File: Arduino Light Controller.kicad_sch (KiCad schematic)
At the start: 26 parts, among them J1 61300411121, J10 61300211121, J11 61300211121, J12 61300211121, J13 61300211121, J14 61300211121, J15 61300211121, J16 61300211121, J17 61300211121, J18 61300211121, J19 61300211121, J2 61300411121, J20 61300211121, J21 61300211121, J22 61300211121, J3 61300411121, J4 61300411121, J5 61300311121, J6 61300311121, J7 61300211121, J8 61300211121, J9 61300211121

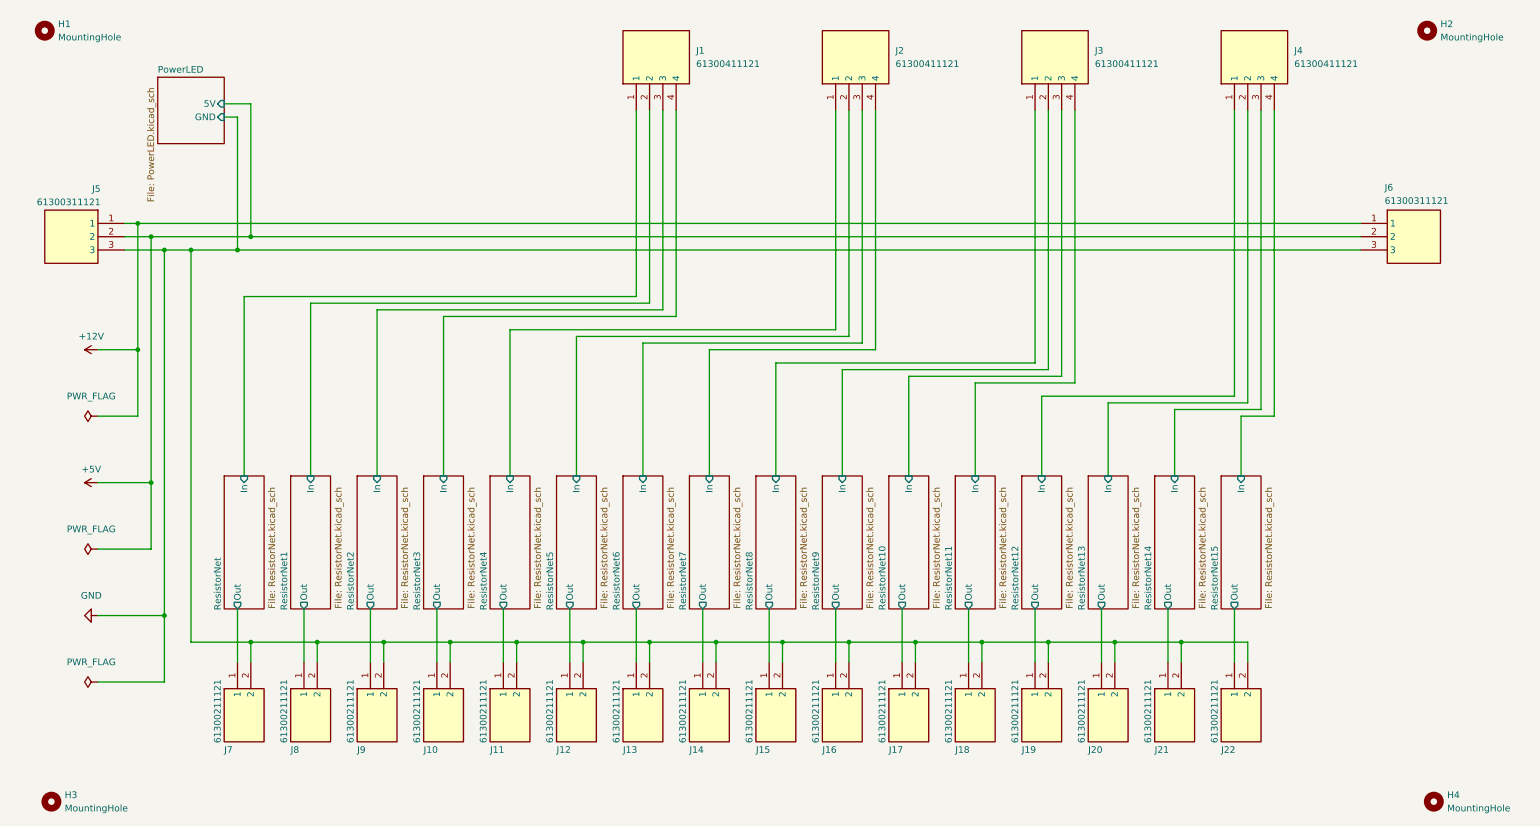
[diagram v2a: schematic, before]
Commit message: Updated re-annotated the schematics, created new PCB based on standards and updated components.
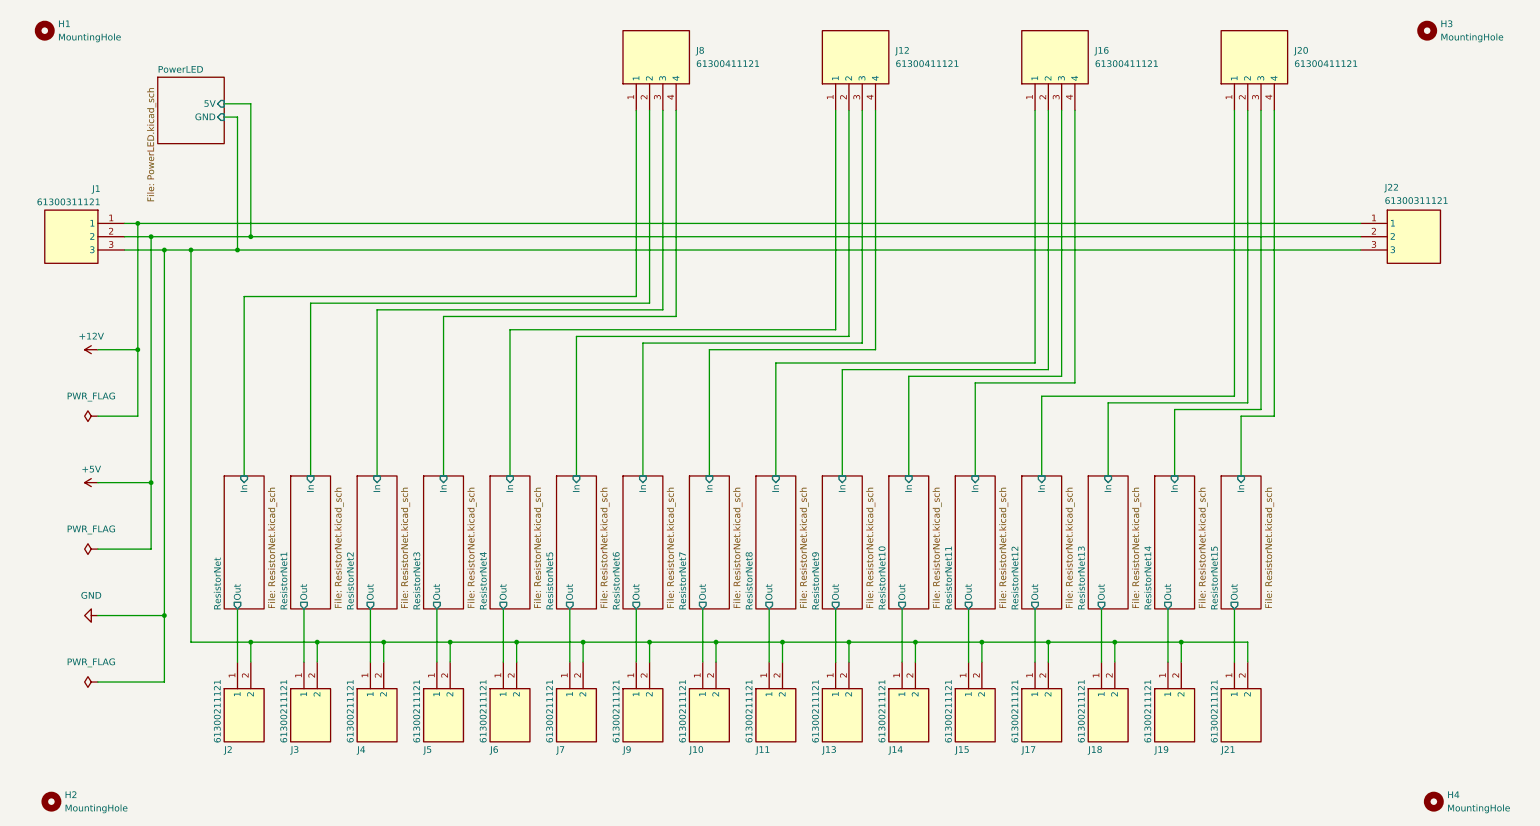
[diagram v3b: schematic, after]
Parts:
- renumbered H3 to H2, H2 to H3, J5 to J1, J14 to J10, J15 to J11, J2 to J12, J16 to J13, J17 to J14, J18 to J15, J3 to J16, J19 to J17, J20 to J18, J21 to J19, J7 to J2, J4 to J20, J22 to J21, J6 to J22, J8 to J3, J9 to J4, J10 to J5, J11 to J6, J12 to J7, J1 to J8, J13 to J9
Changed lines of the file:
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@@
 		(on_board yes)
 		(dnp no)
-		(property "Reference" "J7"
+		(property "Reference" "J2"
 			(at 50.8 153.924 90)
 			(effects
@@
 			(project "Arduino Light Controller"
 				(path "/1ab818d2-1673-4bd5-b77a-2cfddf9e3efa"
-					(reference "J7")
+					(reference "J2")
 					(unit 1)
 				)
@@
 		(on_board yes)
 		(dnp no)
-		(property "Reference" "J13"
+		(property "Reference" "J9"
 			(at 127 153.924 90)
 			(effects
@@
 			(project "Arduino Light Controller"
 				(path "/1ab818d2-1673-4bd5-b77a-2cfddf9e3efa"
-					(reference "J13")
+					(reference "J9")
 					(unit 1)
 				)
@@
 		(on_board yes)
 		(dnp no)
-		(property "Reference" "J10"
+		(property "Reference" "J5"
 			(at 88.9 153.924 90)
 			(effects
@@
 			(project "Arduino Light Controller"
 				(path "/1ab818d2-1673-4bd5-b77a-2cfddf9e3efa"
-					(reference "J10")
+					(reference "J5")
 					(unit 1)
 				)
@@
 		(dnp no)
 		(fields_autoplaced yes)
-		(property "Reference" "#PWR04"
+		(property "Reference" "#PWR02"
 			(at 30.48 102.87 0)
 			(effects
@@
 			(project "Arduino Light Controller"
 				(path "/1ab818d2-1673-4bd5-b77a-2cfddf9e3efa"
-					(reference "#PWR04")
+					(reference "#PWR02")
 					(unit 1)
 				)
@@
 		(on_board yes)
 		(dnp no)
-		(property "Reference" "J11"
+		(property "Reference" "J6"
 			(at 101.6 153.924 90)
 			(effects
@@
 			(project "Arduino Light Controller"
 				(path "/1ab818d2-1673-4bd5-b77a-2cfddf9e3efa"
-					(reference "J11")
+					(reference "J6")
 					(unit 1)
 				)
@@
 		(on_board yes)
 		(dnp no)
-		(property "Reference" "J21"
+		(property "Reference" "J19"
 			(at 228.6 153.924 90)
 			(effects
@@
 			(project "Arduino Light Controller"
 				(path "/1ab818d2-1673-4bd5-b77a-2cfddf9e3efa"
-					(reference "J21")
+					(reference "J19")
 					(unit 1)
 				)
@@
 		(on_board yes)
 		(dnp no)
-		(property "Reference" "J15"
+		(property "Reference" "J11"
 			(at 152.4 153.924 90)
 			(effects
@@
 			(project "Arduino Light Controller"
 				(path "/1ab818d2-1673-4bd5-b77a-2cfddf9e3efa"
-					(reference "J15")
+					(reference "J11")
 					(unit 1)
 				)
@@
 		(on_board yes)
 		(dnp no)
-		(property "Reference" "J19"
+		(property "Reference" "J17"
 			(at 203.2 153.924 90)
 			(effects
@@
 			(project "Arduino Light Controller"
 				(path "/1ab818d2-1673-4bd5-b77a-2cfddf9e3efa"
-					(reference "J19")
+					(reference "J17")
 					(unit 1)
 				)
@@
 		(on_board yes)
 		(dnp no)
-		(property "Reference" "J9"
+		(property "Reference" "J4"
 			(at 76.2 153.924 90)
 			(effects
@@
 			(project "Arduino Light Controller"
 				(path "/1ab818d2-1673-4bd5-b77a-2cfddf9e3efa"
-					(reference "J9")
+					(reference "J4")
 					(unit 1)
 				)
@@
 		(dnp no)
 		(fields_autoplaced yes)
-		(property "Reference" "J3"
+		(property "Reference" "J16"
 			(at 217.17 20.3199 90)
 			(effects
@@
 			(project "Arduino Light Controller"
 				(path "/1ab818d2-1673-4bd5-b77a-2cfddf9e3efa"
-					(reference "J3")
+					(reference "J16")
 					(unit 1)
 				)
@@
 		(on_board yes)
 		(dnp no)
-		(property "Reference" "J5"
+		(property "Reference" "J1"
 			(at 27.178 46.736 0)
 			(effects
@@
 			(project "Arduino Light Controller"
 				(path "/1ab818d2-1673-4bd5-b77a-2cfddf9e3efa"
-					(reference "J5")
+					(reference "J1")
 					(unit 1)
 				)
@@
 		(on_board yes)
 		(dnp no)
-		(property "Reference" "J20"
+		(property "Reference" "J18"
 			(at 215.9 153.924 90)
 			(effects
@@
 			(project "Arduino Light Controller"
 				(path "/1ab818d2-1673-4bd5-b77a-2cfddf9e3efa"
-					(reference "J20")
+					(reference "J18")
 					(unit 1)
 				)
@@
 		(on_board yes)
 		(dnp no)
-		(property "Reference" "J22"
+		(property "Reference" "J21"
 			(at 241.3 153.924 90)
 			(effects
@@
 			(project "Arduino Light Controller"
 				(path "/1ab818d2-1673-4bd5-b77a-2cfddf9e3efa"
-					(reference "J22")
+					(reference "J21")
 					(unit 1)
 				)
@@
 		(on_board yes)
 		(dnp no)
-		(property "Reference" "J17"
+		(property "Reference" "J14"
 			(at 177.8 153.924 90)
 			(effects
@@
 			(project "Arduino Light Controller"
 				(path "/1ab818d2-1673-4bd5-b77a-2cfddf9e3efa"
-					(reference "J17")
+					(reference "J14")
 					(unit 1)
 				)
@@
 		(dnp no)
 		(fields_autoplaced yes)
-		(property "Reference" "J2"
+		(property "Reference" "J12"
 			(at 179.07 20.3199 90)
 			(effects
@@
 			(project "Arduino Light Controller"
 				(path "/1ab818d2-1673-4bd5-b77a-2cfddf9e3efa"
-					(reference "J2")
+					(reference "J12")
 					(unit 1)
 				)
@@
 		(dnp no)
 		(fields_autoplaced yes)
-		(property "Reference" "J1"
+		(property "Reference" "J8"
 			(at 140.97 20.3199 90)
 			(effects
@@
 			(project "Arduino Light Controller"
 				(path "/1ab818d2-1673-4bd5-b77a-2cfddf9e3efa"
-					(reference "J1")
+					(reference "J8")
 					(unit 1)
 				)
@@
 		(on_board yes)
 		(dnp no)
-		(property "Reference" "J18"
+		(property "Reference" "J15"
 			(at 190.5 153.924 90)
 			(effects
@@
 			(project "Arduino Light Controller"
 				(path "/1ab818d2-1673-4bd5-b77a-2cfddf9e3efa"
-					(reference "J18")
+					(reference "J15")
 					(unit 1)
 				)
@@
 		(dnp no)
 		(fields_autoplaced yes)
-		(property "Reference" "J4"
+		(property "Reference" "J20"
 			(at 255.27 20.3199 90)
 			(effects
@@
 			(project "Arduino Light Controller"
 				(path "/1ab818d2-1673-4bd5-b77a-2cfddf9e3efa"
-					(reference "J4")
+					(reference "J20")
 					(unit 1)
 				)
@@
 		(on_board yes)
 		(dnp no)
-		(property "Reference" "J14"
+		(property "Reference" "J10"
 			(at 139.7 153.924 90)
 			(effects
@@
 			(project "Arduino Light Controller"
 				(path "/1ab818d2-1673-4bd5-b77a-2cfddf9e3efa"
-					(reference "J14")
+					(reference "J10")
 					(unit 1)
 				)
@@
 		(dnp no)
 		(fields_autoplaced yes)
-		(property "Reference" "#PWR02"
+		(property "Reference" "#PWR01"
 			(at 30.48 77.47 0)
 			(effects
@@
 			(project "Arduino Light Controller"
 				(path "/1ab818d2-1673-4bd5-b77a-2cfddf9e3efa"
-					(reference "#PWR02")
+					(reference "#PWR01")
 					(unit 1)
 				)
@@
 		(on_board yes)
 		(dnp no)
-		(property "Reference" "J12"
+		(property "Reference" "J7"
 			(at 114.3 153.924 90)
 			(effects
@@
 			(project "Arduino Light Controller"
 				(path "/1ab818d2-1673-4bd5-b77a-2cfddf9e3efa"
-					(reference "J12")
+					(reference "J7")
 					(unit 1)
 				)
@@
 		(on_board yes)
 		(dnp no)
-		(property "Reference" "J8"
+		(property "Reference" "J3"
 			(at 63.5 153.924 90)
 			(effects
@@
 			(project "Arduino Light Controller"
 				(path "/1ab818d2-1673-4bd5-b77a-2cfddf9e3efa"
-					(reference "J8")
+					(reference "J3")
 					(unit 1)
 				)
@@
 		(on_board yes)
 		(dnp no)
-		(property "Reference" "J16"
+		(property "Reference" "J13"
 			(at 165.1 153.924 90)
 			(effects
@@
 			(project "Arduino Light Controller"
 				(path "/1ab818d2-1673-4bd5-b77a-2cfddf9e3efa"
-					(reference "J16")
+					(reference "J13")
 					(unit 1)
 				)
@@
 		(dnp no)
 		(fields_autoplaced yes)
-		(property "Reference" "H2"
+		(property "Reference" "H3"
 			(at 283.21 15.2399 0)
 			(effects
@@
 			(project "Arduino Light Controller"
 				(path "/1ab818d2-1673-4bd5-b77a-2cfddf9e3efa"
-					(reference "H2")
+					(reference "H3")
 					(unit 1)
 				)
@@
 		(on_board yes)
 		(dnp no)
-		(property "Reference" "J6"
+		(property "Reference" "J22"
 			(at 272.542 46.482 0)
 			(effects
@@
 			(project "Arduino Light Controller"
 				(path "/1ab818d2-1673-4bd5-b77a-2cfddf9e3efa"
-					(reference "J6")
+					(reference "J22")
 					(unit 1)
 				)
@@
 		(dnp no)
 		(fields_autoplaced yes)
-		(property "Reference" "H3"
+		(property "Reference" "H2"
 			(at 20.32 162.5599 0)
 			(effects
@@
 			(project "Arduino Light Controller"
 				(path "/1ab818d2-1673-4bd5-b77a-2cfddf9e3efa"
-					(reference "H3")
+					(reference "H2")
 					(unit 1)
 				)

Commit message: Updated components to the custom library and applied additional standards.
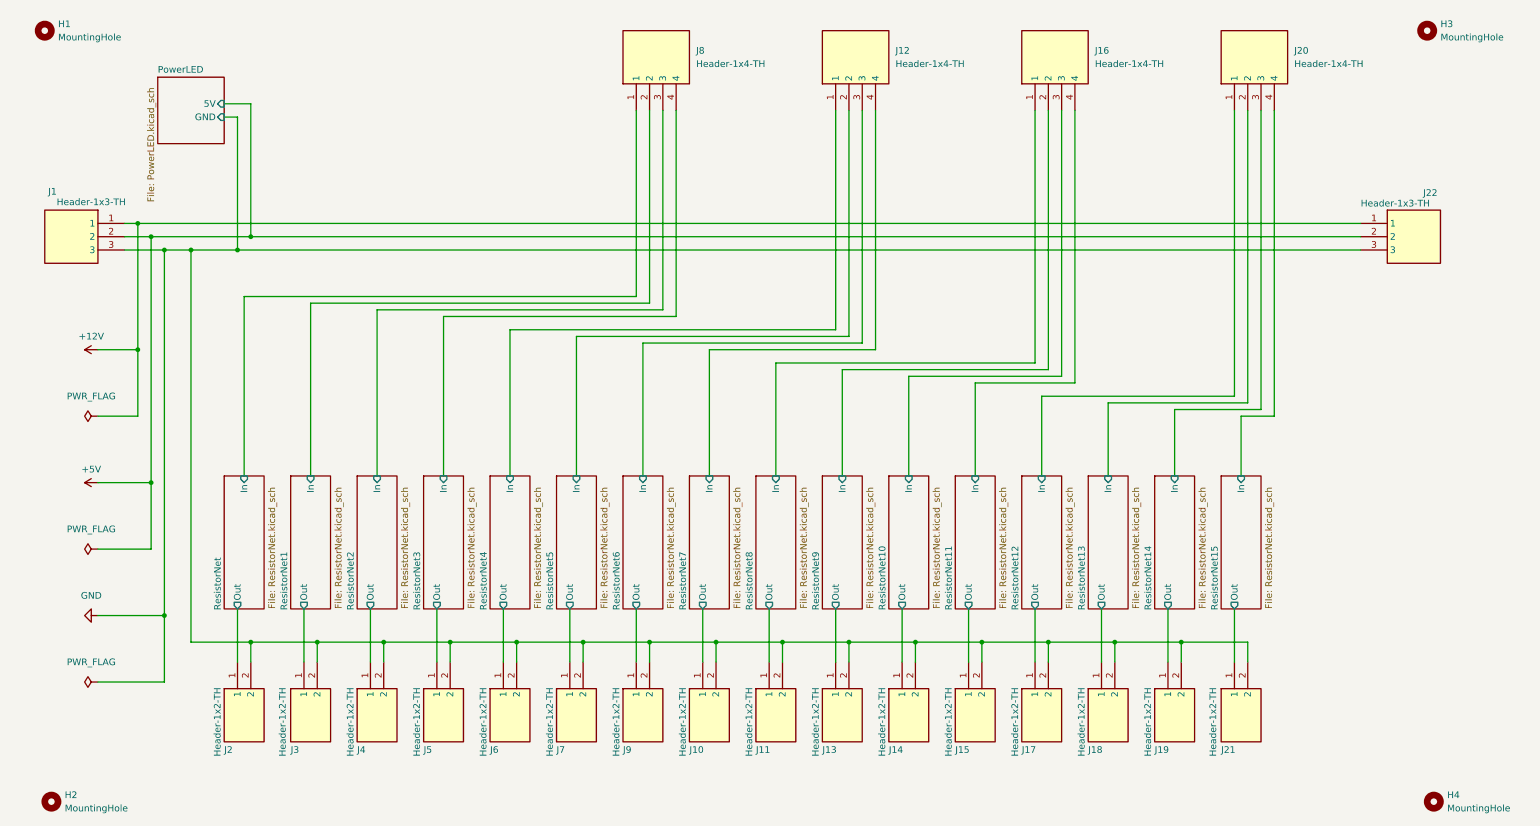
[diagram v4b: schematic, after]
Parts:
- J1, J22: value 61300311121 -> Header-1x3-TH; footprint SamacSys_Parts:HDRV3W64P0X254_1X3_762X254X869P -> Custom:710-61300311121; symbol SamacSys_Parts:61300311121 -> Custom:Header-1x3-TH; Supplier (none) -> Mouser; Supplier Part Number (none) -> 710-61300311121; Supplier Price/Stock (none) -> https://www.mouser.co.uk/ProductDetail/Wurth-Elektronik/613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
- J10, J11, J13, J14, J15, J17, J18, J19, J2, J21, J3, J4, J5, J6, J7, J9: value 61300211121 -> Header-1x2-TH; footprint SamacSys_Parts:HDRV2W110P0X254_1X2_508X254X854P -> Custom:710-61300211121; symbol SamacSys_Parts:61300211121 -> Custom:Header-1x2-TH; Supplier (none) -> Mouser; Supplier Part Number (none) -> 710-61300211121; Supplier Price/Stock (none) -> https://www.mouser.co.uk/ProductDetail/Wurth-Elektronik/613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
- J12, J16, J20, J8: value 61300411121 -> Header-1x4-TH; footprint SamacSys_Parts:HDRV4W95P0X254_1X4_1016X254X854P -> Custom:710-61300411121; symbol SamacSys_Parts:61300411121 -> Custom:Header-1x4-TH; Supplier (none) -> Mouser; Supplier Part Number (none) -> 710-61300411121; Supplier Price/Stock (none) -> https://www.mouser.co.uk/ProductDetail/Wurth-Elektronik/613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

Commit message: Updated sheets with title, version, and date.  Corrected issue with resistor placement and connection on PowerLED module.
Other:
- title: (none) -> Arduino Light Controller
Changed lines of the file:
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@@
 	(generator_version "9.0")
 	(paper "A4")
+	(title_block
+		(title "Arduino Light Controller")
+		(date "2026-01-30")
+		(rev "1.1")
+	)
 	(junction
 		(at 208.28 133.35)
